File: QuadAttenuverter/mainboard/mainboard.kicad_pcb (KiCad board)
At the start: 2 copper layers, 35.6 x 108 mm, 64 parts, among them J1 Conn_01x09, J2 Conn_02x10_Counter_Clockwise, J3 Conn_02x05_Odd_Even, U1 LM324, U2 LM324, U3 LM324, U4 LM324, U5 LM324

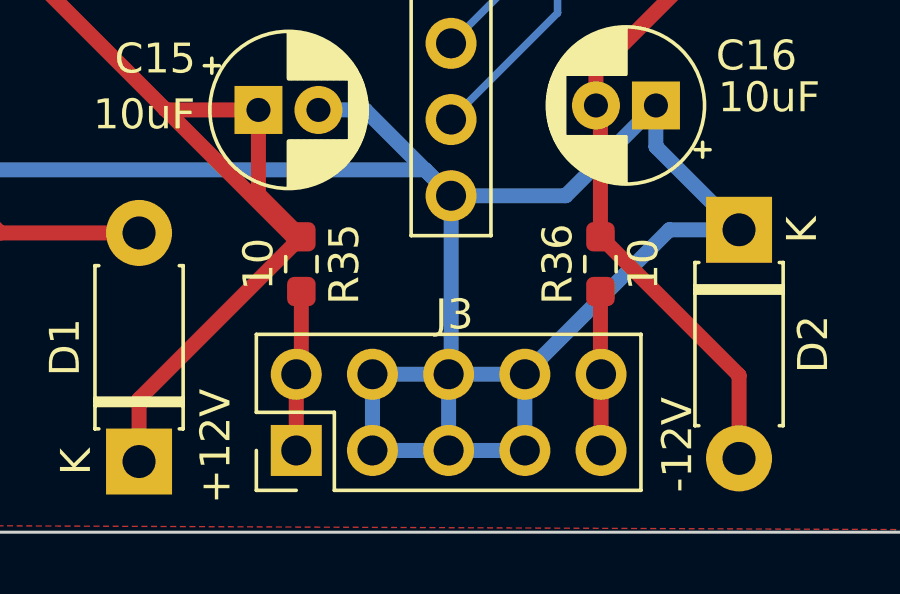
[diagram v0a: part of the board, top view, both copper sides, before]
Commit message: Update power connector graphics
To make it clear how 10-pin IDC connector would be placed w.r.t. +12 and -12.
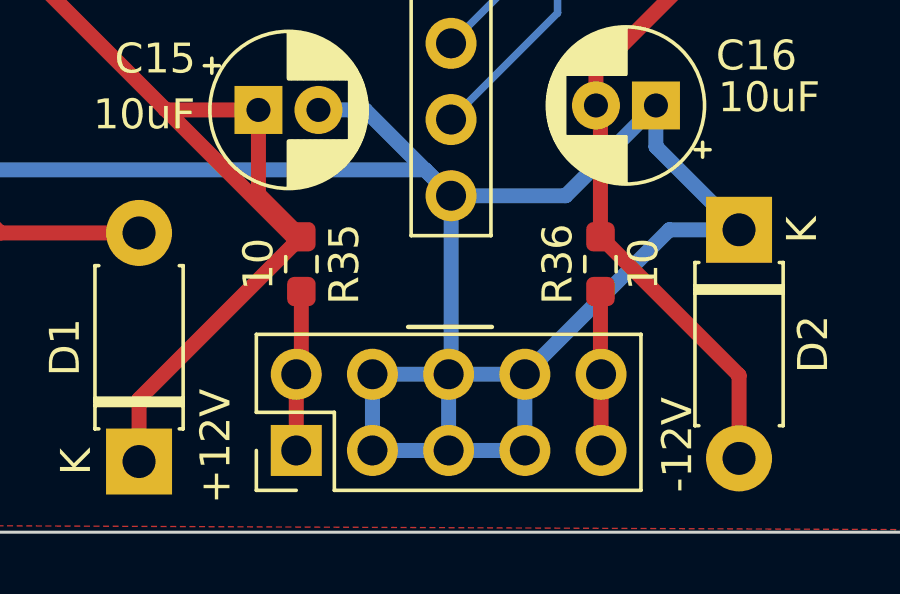
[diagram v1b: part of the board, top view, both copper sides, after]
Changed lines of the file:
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@@
     (property "Sheetname" "")
     (attr through_hole)
-    (fp_text reference "J3" (at 4.53 5.27 180) (layer "F.SilkS")
+    (fp_text reference "J3" (at 4.53 5.27 180) (layer "F.Fab")
       (effects (font (size 1 1) (thickness 0.15)))
     )
@@
   (gr_line (start 104.7 86.225) (end 104.7 82.2) (layer "F.SilkS") (width 0.15))
   (gr_line (start 88.175 105.775) (end 95.85 105.775) (layer "F.SilkS") (width 0.15))
+  (gr_line (start 99.568 140.462) (end 102.362 140.462) (layer "F.SilkS") (width 0.15))
   (gr_line (start 104.675 105.975) (end 104.675 102.95) (layer "F.SilkS") (width 0.15))
   (gr_line (start 104.175 86.225) (end 111.625 86.225) (layer "F.SilkS") (width 0.15))

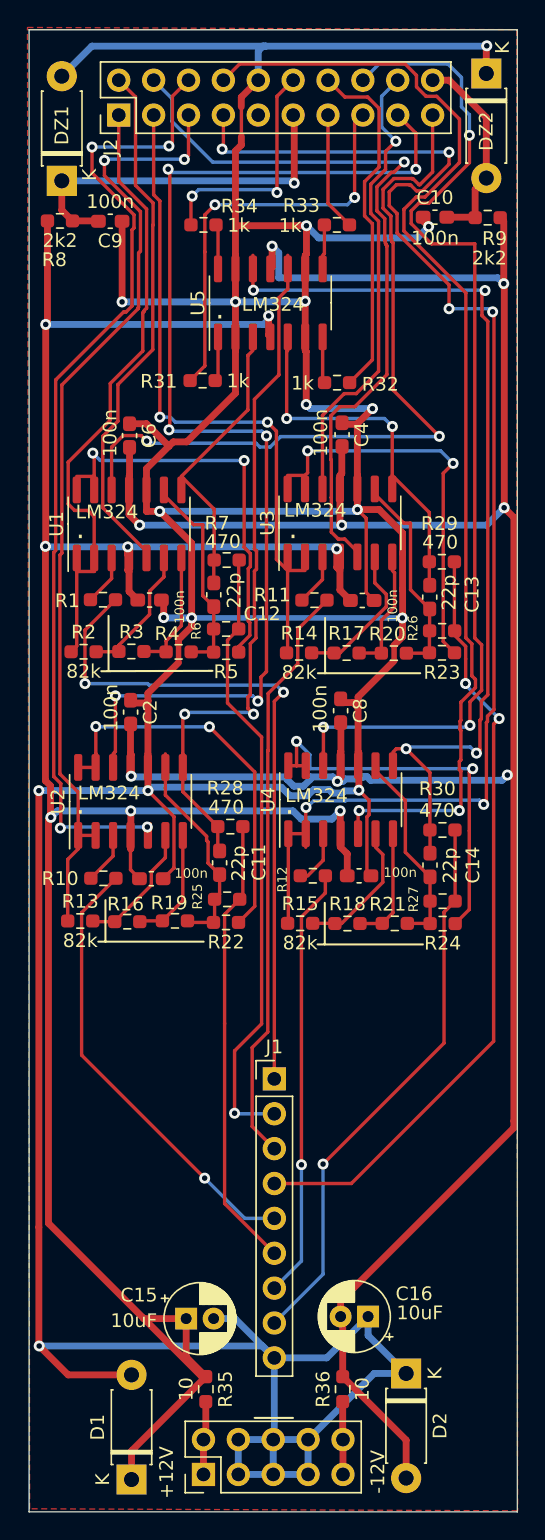
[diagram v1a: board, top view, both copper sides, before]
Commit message: Add M3 mount for mechanical stability, and update power
If pots are used that don't have mounting brackets, the faceplate needs
extra mechanical support at the top. Two M3 screws can support that.

In addition, bottom silk screen is added for the power connector, since
it's probably going to be mounted there.
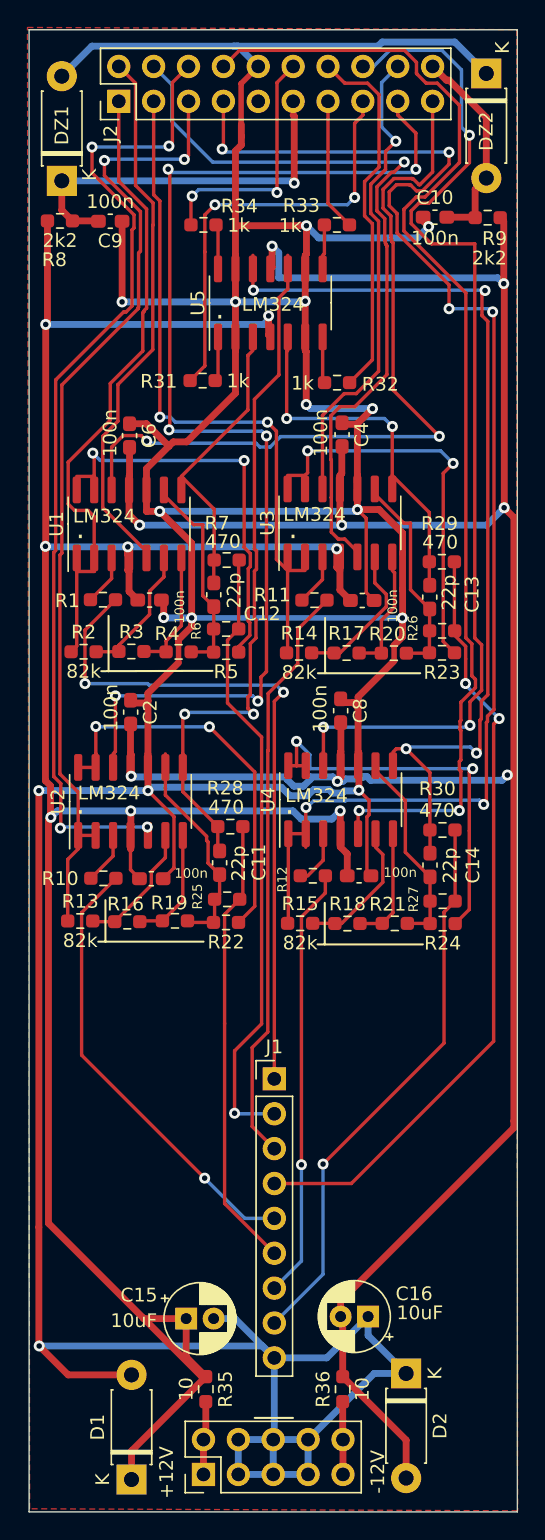
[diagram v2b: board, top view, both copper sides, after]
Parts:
- moved J2 1.00 mm to (89.7, 44.6)
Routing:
- net /LED2: track 25.9 -> 26.9 mm
- net /OFFSET3: track 83.5 -> 84.5 mm
- net /OFFSET2: track 33.1 -> 34.1 mm
- net /OFFSET1: track 55.4 -> 56.4 mm
- net /LED4: track 17.3 -> 18.3 mm
- net /LED3: track 8.65 -> 9.65 mm
- net /LED1: track 30.2 -> 31.2 mm
- net /GAIN4IN: track 98.4 -> 99.4 mm
- net /GAIN3OUT: track 71.0 -> 72.0 mm
- net /GAIN3IN: track 70.3 -> 71.3 mm
- net /GAIN2OUT: track 55.1 -> 56.1 mm
- net /GAIN2IN: track 48.9 -> 49.9 mm
- net /GAIN1OUT: track 38.2 -> 39.2 mm
- net /GAIN1IN: track 45.1 -> 46.1 mm
- net /GAIN4OUT: track 84.0 -> 85.0 mm
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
